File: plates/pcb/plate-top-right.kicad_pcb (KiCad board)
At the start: 2 copper layers, 125.1 x 92.6 mm, 0 parts

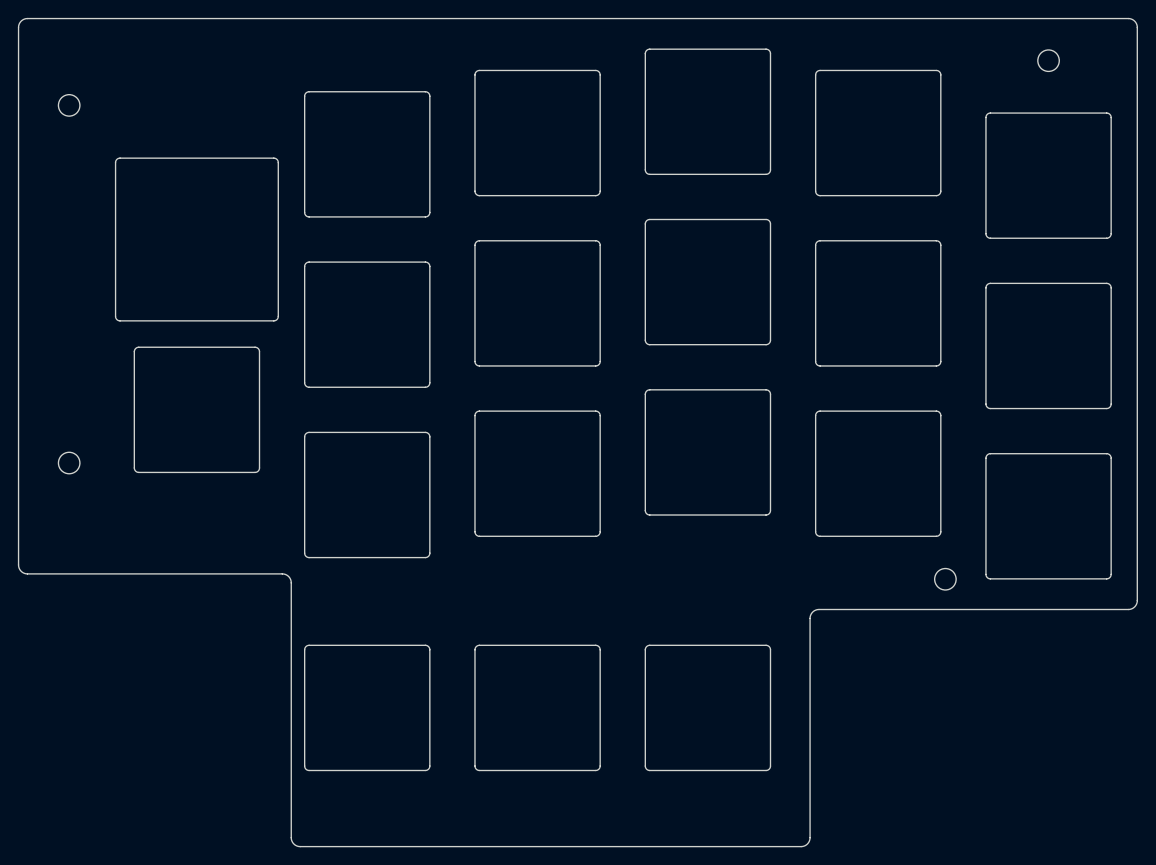
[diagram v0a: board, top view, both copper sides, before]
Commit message: fix(cad): update Z-stackup, 6mm cup standoffs, cup ear/plate clearances, ceramic ball throat, and sensor/CKW12 models
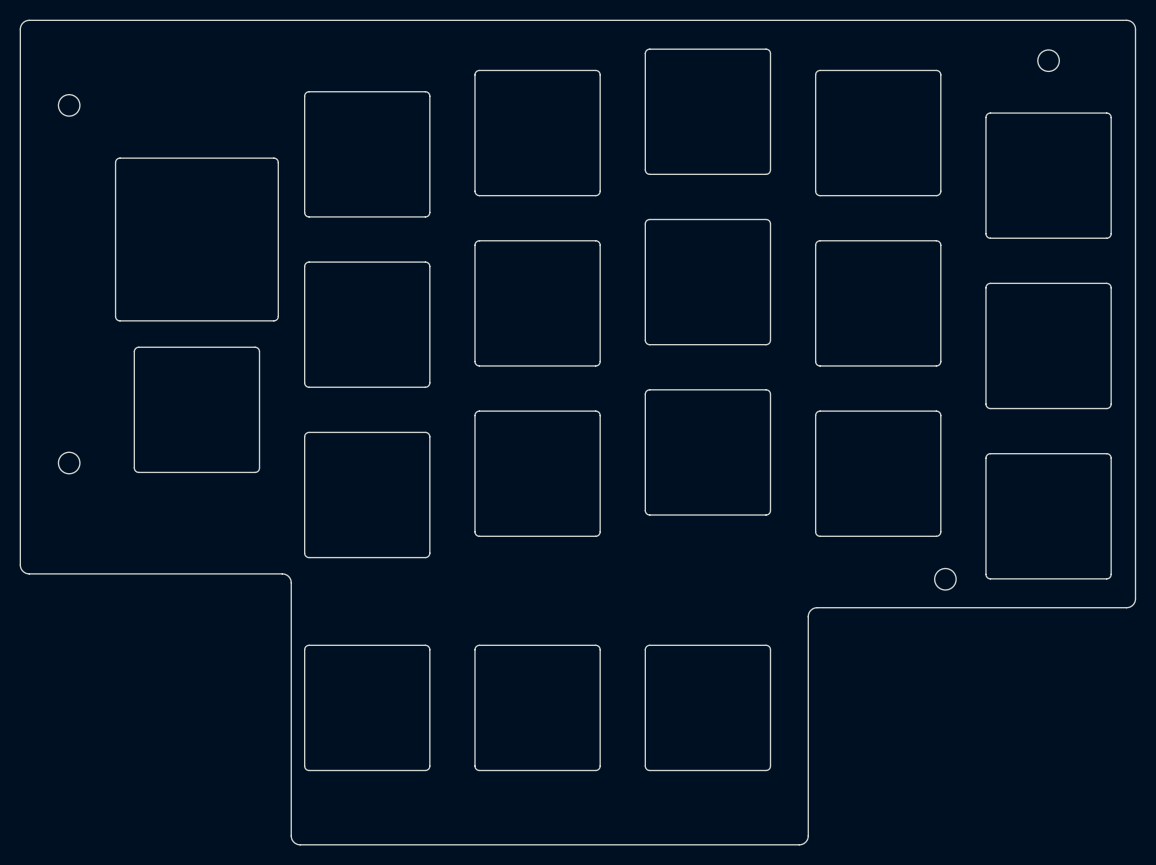
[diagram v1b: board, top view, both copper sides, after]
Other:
- board size 125.1 x 92.6 mm -> 124.7 x 92.2 mm
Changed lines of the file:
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@@
 	)
 	(gr_arc
-		(start -5.6625 -23.7125)
-		(mid -5.369607 -24.419607)
-		(end -4.6625 -24.7125)
-		(stroke
-			(width 0.15)
-			(type default)
-		)
-		(layer "Edge.Cuts")
-	)
-	(gr_line
-		(start -5.6625 36.4)
-		(end -5.6625 -23.7125)
-		(stroke
-			(width 0.15)
-			(type default)
-		)
-		(layer "Edge.Cuts")
-	)
-	(gr_line
-		(start -4.6625 -24.7125)
-		(end 118.4625 -24.7125)
-		(stroke
-			(width 0.15)
-			(type default)
-		)
-		(layer "Edge.Cuts")
-	)
-	(gr_arc
-		(start -4.6625 37.4)
-		(mid -5.369607 37.107107)
-		(end -5.6625 36.4)
+		(start -5.4625 -23.5125)
+		(mid -5.169607 -24.219607)
+		(end -4.4625 -24.5125)
+		(stroke
+			(width 0.15)
+			(type default)
+		)
+		(layer "Edge.Cuts")
+	)
+	(gr_line
+		(start -5.4625 36.4)
+		(end -5.4625 -23.5125)
+		(stroke
+			(width 0.15)
+			(type default)
+		)
+		(layer "Edge.Cuts")
+	)
+	(gr_line
+		(start -4.4625 -24.5125)
+		(end 118.2625 -24.5125)
+		(stroke
+			(width 0.15)
+			(type default)
+		)
+		(layer "Edge.Cuts")
+	)
+	(gr_arc
+		(start -4.4625 37.4)
+		(mid -5.169607 37.107107)
+		(end -5.4625 36.4)
 		(stroke
 			(width 0.15)
@@
 	(gr_line
 		(start 23.8375 37.4)
-		(end -4.6625 37.4)
+		(end -4.4625 37.4)
 		(stroke
 			(width 0.15)
@@
 	)
 	(gr_line
-		(start 24.8375 66.9)
+		(start 24.8375 66.7)
 		(end 24.8375 38.4)
 		(stroke
@@
 	)
 	(gr_arc
-		(start 25.8375 67.9)
-		(mid 25.130393 67.607107)
-		(end 24.8375 66.9)
+		(start 25.8375 67.7)
+		(mid 25.130393 67.407107)
+		(end 24.8375 66.7)
 		(stroke
 			(width 0.15)
@@
 	)
 	(gr_line
-		(start 81.8625 67.9)
-		(end 25.8375 67.9)
-		(stroke
-			(width 0.15)
-			(type default)
-		)
-		(layer "Edge.Cuts")
-	)
-	(gr_line
-		(start 82.8625 42.38125)
-		(end 82.8625 66.9)
-		(stroke
-			(width 0.15)
-			(type default)
-		)
-		(layer "Edge.Cuts")
-	)
-	(gr_arc
-		(start 82.8625 42.38125)
-		(mid 83.155376 41.674111)
-		(end 83.8625 41.38125)
-		(stroke
-			(width 0.15)
-			(type default)
-		)
-		(layer "Edge.Cuts")
-	)
-	(gr_arc
-		(start 82.8625 66.9)
-		(mid 82.569607 67.607107)
-		(end 81.8625 67.9)
+		(start 81.6625 67.7)
+		(end 25.8375 67.7)
+		(stroke
+			(width 0.15)
+			(type default)
+		)
+		(layer "Edge.Cuts")
+	)
+	(gr_line
+		(start 82.6625 42.18125)
+		(end 82.6625 66.7)
+		(stroke
+			(width 0.15)
+			(type default)
+		)
+		(layer "Edge.Cuts")
+	)
+	(gr_arc
+		(start 82.6625 42.18125)
+		(mid 82.955376 41.474111)
+		(end 83.6625 41.18125)
+		(stroke
+			(width 0.15)
+			(type default)
+		)
+		(layer "Edge.Cuts")
+	)
+	(gr_arc
+		(start 82.6625 66.7)
+		(mid 82.369607 67.407107)
+		(end 81.6625 67.7)
 		(stroke
 			(width 0.15)
@@
 	)
 	(gr_arc
-		(start 118.4625 -24.7125)
-		(mid 119.169607 -24.419607)
-		(end 119.4625 -23.7125)
-		(stroke
-			(width 0.15)
-			(type default)
-		)
-		(layer "Edge.Cuts")
-	)
-	(gr_line
-		(start 118.4625 41.38125)
-		(end 83.8625 41.38125)
-		(stroke
-			(width 0.15)
-			(type default)
-		)
-		(layer "Edge.Cuts")
-	)
-	(gr_line
-		(start 119.4625 -23.7125)
-		(end 119.4625 40.38125)
-		(stroke
-			(width 0.15)
-			(type default)
-		)
-		(layer "Edge.Cuts")
-	)
-	(gr_arc
-		(start 119.4625 40.38125)
-		(mid 119.169607 41.088357)
-		(end 118.4625 41.38125)
-		(stroke
-			(width 0.15)
+		(start 118.2625 -24.5125)
+		(mid 118.969607 -24.219607)
+		(end 119.2625 -23.5125)
+		(stroke
+			(width 0.15)
+			(type default)
+		)
+		(layer "Edge.Cuts")
+	)
+	(gr_line
+		(start 118.2625 41.18125)
+		(end 83.6625 41.18125)
+		(stroke
+			(width 0.15)
+			(type default)
+		)
+		(layer "Edge.Cuts")
+	)
+	(gr_line
+		(start 119.2625 -23.5125)
+		(end 119.2625 40.18125)
+		(stroke
+			(width 0.15)
+			(type default)
+		)
+		(layer "Edge.Cuts")
+	)
+	(gr_arc
+		(start 119.2625 40.18125)
+		(mid 118.969607 40.888357)
+		(end 118.2625 41.18125)
+		(stroke
+			(width 0.15)

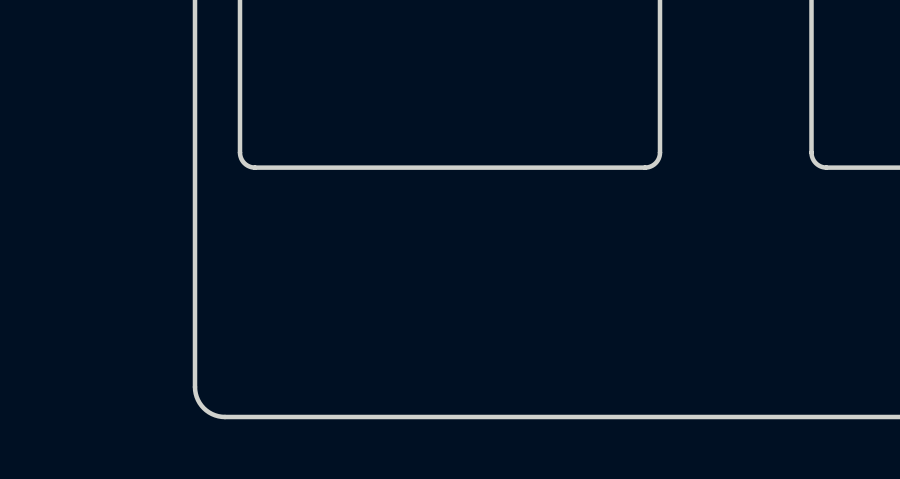
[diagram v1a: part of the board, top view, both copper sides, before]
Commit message: feat(pcb): separate pmw3360 sensor PCB with JST SH 6-pin connector and add symmetric thumb mounting holes L5/R5
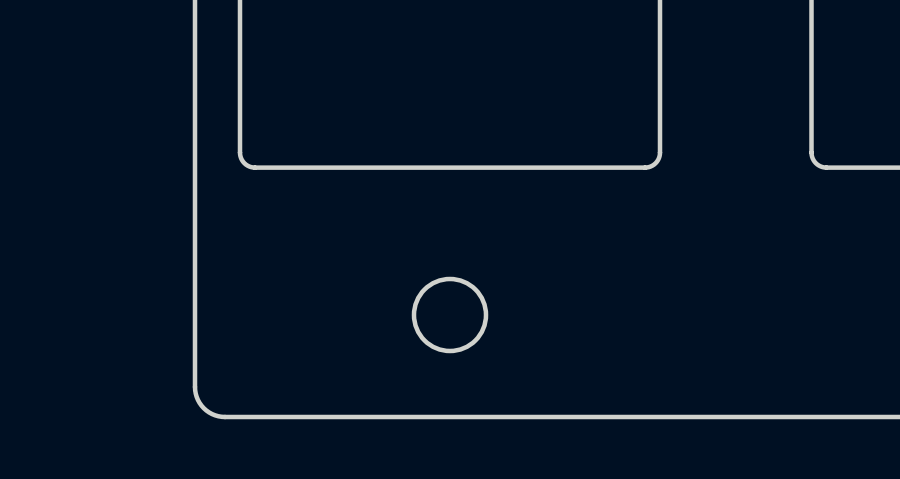
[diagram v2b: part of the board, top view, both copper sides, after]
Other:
- outline, holes or cut-outs redrawn
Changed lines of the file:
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@@
+		(layer "Edge.Cuts")
+	)
+	(gr_circle
+		(center 33.3375 64.3)
+		(end 34.5375 64.3)
+		(stroke
+			(width 0.15)
+			(type default)
+		)
+		(fill no)
 		(layer "Edge.Cuts")
 	)

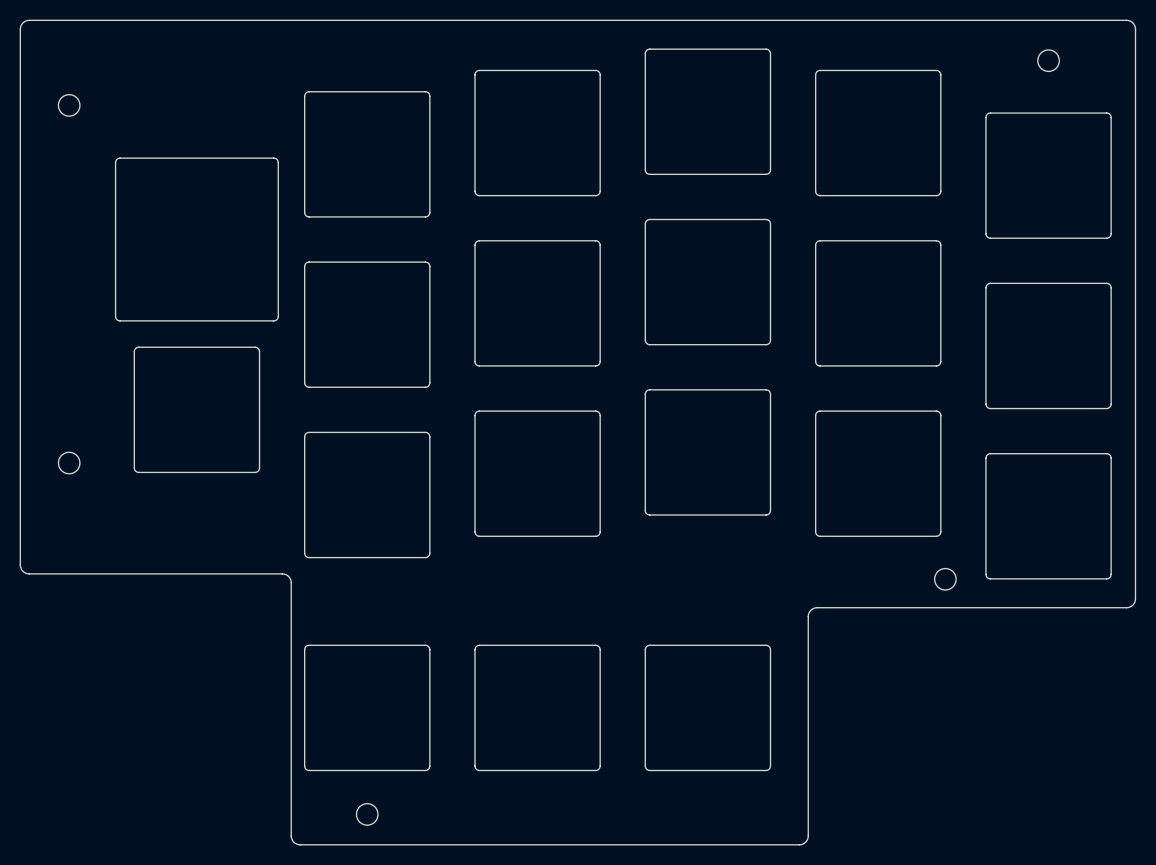
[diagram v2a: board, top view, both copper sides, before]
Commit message: feat(pcb,plates): face-to-face JST SH orientation, move TRRS jack north, and refine mounting holes
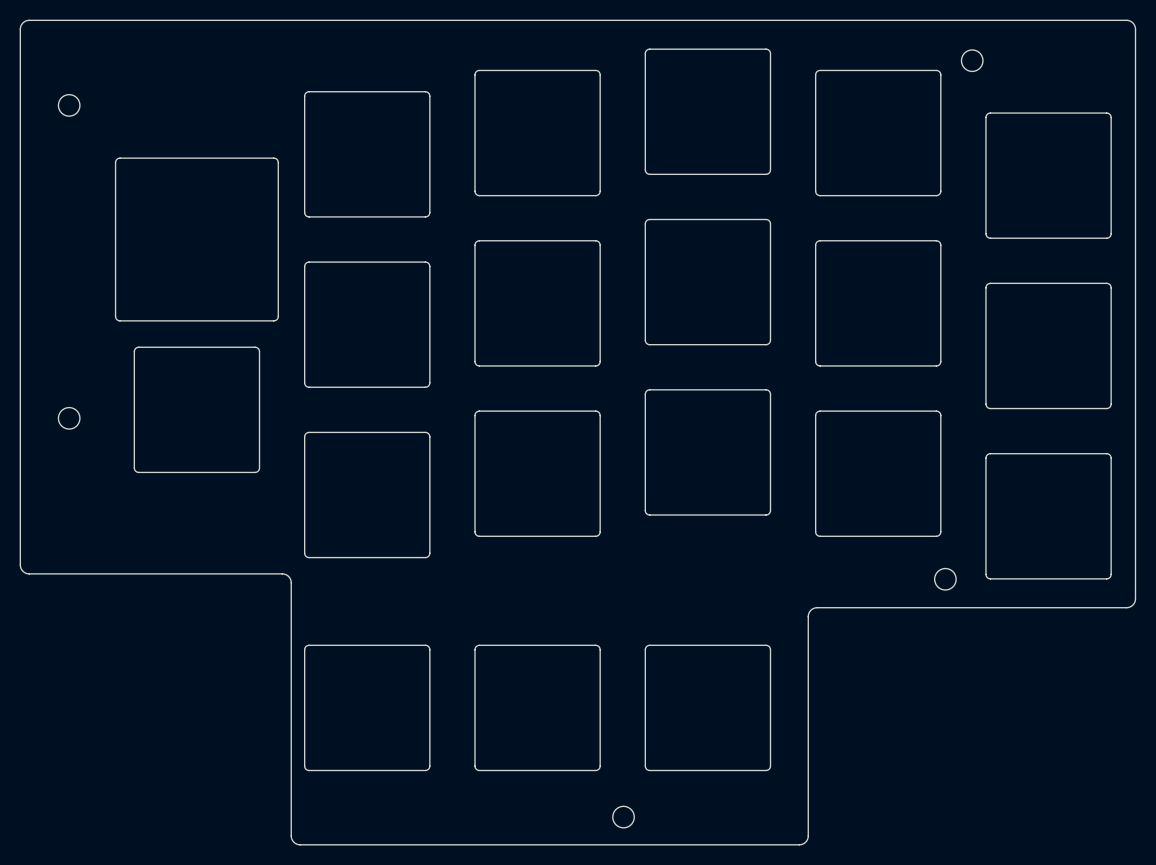
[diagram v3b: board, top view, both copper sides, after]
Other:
- outline, holes or cut-outs redrawn
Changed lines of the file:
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@@
 	)
 	(gr_circle
-		(center 0 25)
-		(end 1.2 25)
+		(center 0 20)
+		(end 1.2 20)
 		(stroke
 			(width 0.15)
@@
 		(layer "Edge.Cuts")
 	)
-	(gr_circle
-		(center 33.3375 64.3)
-		(end 34.5375 64.3)
-		(stroke
-			(width 0.15)
-			(type default)
-		)
-		(fill no)
-		(layer "Edge.Cuts")
-	)
 	(gr_arc
 		(start 39.8375 -16.524999)
@@
 		(layer "Edge.Cuts")
 	)
+	(gr_circle
+		(center 62 64.599999)
+		(end 63.2 64.599999)
+		(stroke
+			(width 0.15)
+			(type default)
+		)
+		(fill no)
+		(layer "Edge.Cuts")
+	)
 	(gr_arc
 		(start 64.4375 -20.7875)
@@
 		(layer "Edge.Cuts")
 	)
+	(gr_circle
+		(center 101 -20)
+		(end 102.2 -20)
+		(stroke
+			(width 0.15)
+			(type default)
+		)
+		(fill no)
+		(layer "Edge.Cuts")
+	)
 	(gr_arc
 		(start 102.5375 -13.64375)
@@
 		(layer "Edge.Cuts")
 	)
-	(gr_circle
-		(center 109.5375 -20)
-		(end 110.7375 -20)
-		(stroke
-			(width 0.15)
-			(type default)
-		)
-		(fill no)
-		(layer "Edge.Cuts")
-	)
